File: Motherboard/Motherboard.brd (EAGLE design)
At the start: 87.5 x 150 mm, 11 parts

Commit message: refactor
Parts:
- moved J2 54.6 mm to (7.00, 127.0)
- moved J1 39.3 mm to (11.5, 95.5)
- moved U$1 39.3 mm to (19.7, 64.0)
- moved ARDUINO_NANO1 18.5 mm to (47.3, 74.8), turned to 90 degrees
- moved GPS2 6.32 mm to (53.4, 134.1)
- moved IMU 6.32 mm to (37.9, 110.2)
- moved R_SCL 6.32 mm to (16.4, 123.7)
- moved U$3 6.32 mm to (23.7, 123.9)
- moved U$4 6.32 mm to (23.7, 144.2)
- moved ALTIMETER2 6.32 mm to (29.0, 110.7)
- moved R_SDA 6.32 mm to (16.4, 126.9)
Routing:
- added copper zone on layer 1, net GND

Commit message: wip
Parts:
- added AIR_BRAKE: (no value), SparkFun-Connectors:1X03
- renumbered J2 to POWER_IN
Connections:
- removed net VIN: ARDUINO_NANO1.15
- new net N$3: AIR_BRAKE.2, ARDUINO_NANO1.15, POWER_IN.1
- new net N$4: AIR_BRAKE.3, ARDUINO_NANO1.24
- net GND: now also AIR_BRAKE.1, POWER_IN.2
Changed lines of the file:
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@@
 <?xml version="1.0" encoding="utf-8"?>
 <!DOCTYPE eagle SYSTEM "eagle.dtd">
-<eagle version="9.3.0">
+<eagle version="9.3.1">
 <drawing>
 <settings>
@@
 <attribute name="VALUE" x="10.23" y="93.087" size="0.6096" layer="27" font="vector" ratio="20"/>
 </element>
-<element name="J2" library="SparkFun-Connectors" package="SCREWTERMINAL-3.5MM-2" value="" x="7" y="127" smashed="yes" rot="R270">
+<element name="POWER_IN" library="SparkFun-Connectors" package="SCREWTERMINAL-3.5MM-2" value="" x="7" y="127" smashed="yes" rot="R270">
 <attribute name="NAME" x="9.54" y="128.27" size="0.6096" layer="25" font="vector" ratio="20" rot="R270"/>
 <attribute name="PROD_ID" value="CONN-08399" x="7" y="127" size="1.778" layer="27" rot="R270" display="off"/>
 <attribute name="VALUE" x="8.27" y="128.27" size="0.6096" layer="27" font="vector" ratio="20" rot="R270"/>
+</element>
+<element name="AIR_BRAKE" library="SparkFun-Connectors" package="1X03" value="" x="39.5" y="45" smashed="yes">
+<attribute name="NAME" x="38.23" y="46.397" size="0.6096" layer="25" font="vector" ratio="20"/>
+<attribute name="PROD_ID" value="XXX-00000" x="39.5" y="45" size="1.778" layer="27" display="off"/>
+<attribute name="VALUE" x="38.23" y="42.968" size="0.6096" layer="27" font="vector" ratio="20"/>
 </element>
 </elements>
@@
 <vertex x="0" y="0"/>
 </polygon>
+<contactref element="POWER_IN" pad="2"/>
+<contactref element="AIR_BRAKE" pad="1"/>
+<wire x1="40.41" y1="112.52" x2="53.378" y2="129.01" width="0" layer="19" extent="1-1"/>
 <wire x1="29.013" y1="110.69" x2="40.41" y2="112.52" width="0" layer="19" extent="1-1"/>
+<wire x1="7" y1="123.5" x2="29.013" y2="110.69" width="0" layer="19" extent="1-1"/>
+<wire x1="54.96" y1="87.51" x2="40.41" y2="112.52" width="0" layer="19" extent="1-1"/>
+<wire x1="39.72" y1="82.43" x2="54.96" y2="87.51" width="0" layer="19" extent="1-1"/>
+<wire x1="39.5" y1="45" x2="39.72" y2="82.43" width="0" layer="19" extent="1-1"/>
 </signal>
 <signal name="5V">
 <contactref element="ARDUINO_NANO1" pad="12"/>
-</signal>
-<signal name="VIN">
-<contactref element="ARDUINO_NANO1" pad="15"/>
 </signal>
 <signal name="3V3">
@@
 <wire x1="54.96" y1="74.81" x2="40.39" y2="117.43" width="0" layer="19" extent="1-1"/>
 </signal>
+<signal name="N$3">
+<contactref element="AIR_BRAKE" pad="2"/>
+<contactref element="POWER_IN" pad="1"/>
+<contactref element="ARDUINO_NANO1" pad="15"/>
+<wire x1="7" y1="127" x2="54.96" y2="90.05" width="0" layer="19" extent="1-1"/>
+<wire x1="42.04" y1="45" x2="54.96" y2="90.05" width="0" layer="19" extent="1-1"/>
+</signal>
+<signal name="N$4">
+<contactref element="AIR_BRAKE" pad="3"/>
+<contactref element="ARDUINO_NANO1" pad="24"/>
+<wire x1="44.58" y1="45" x2="39.72" y2="69.73" width="0" layer="19" extent="1-1"/>
+</signal>
 </signals>

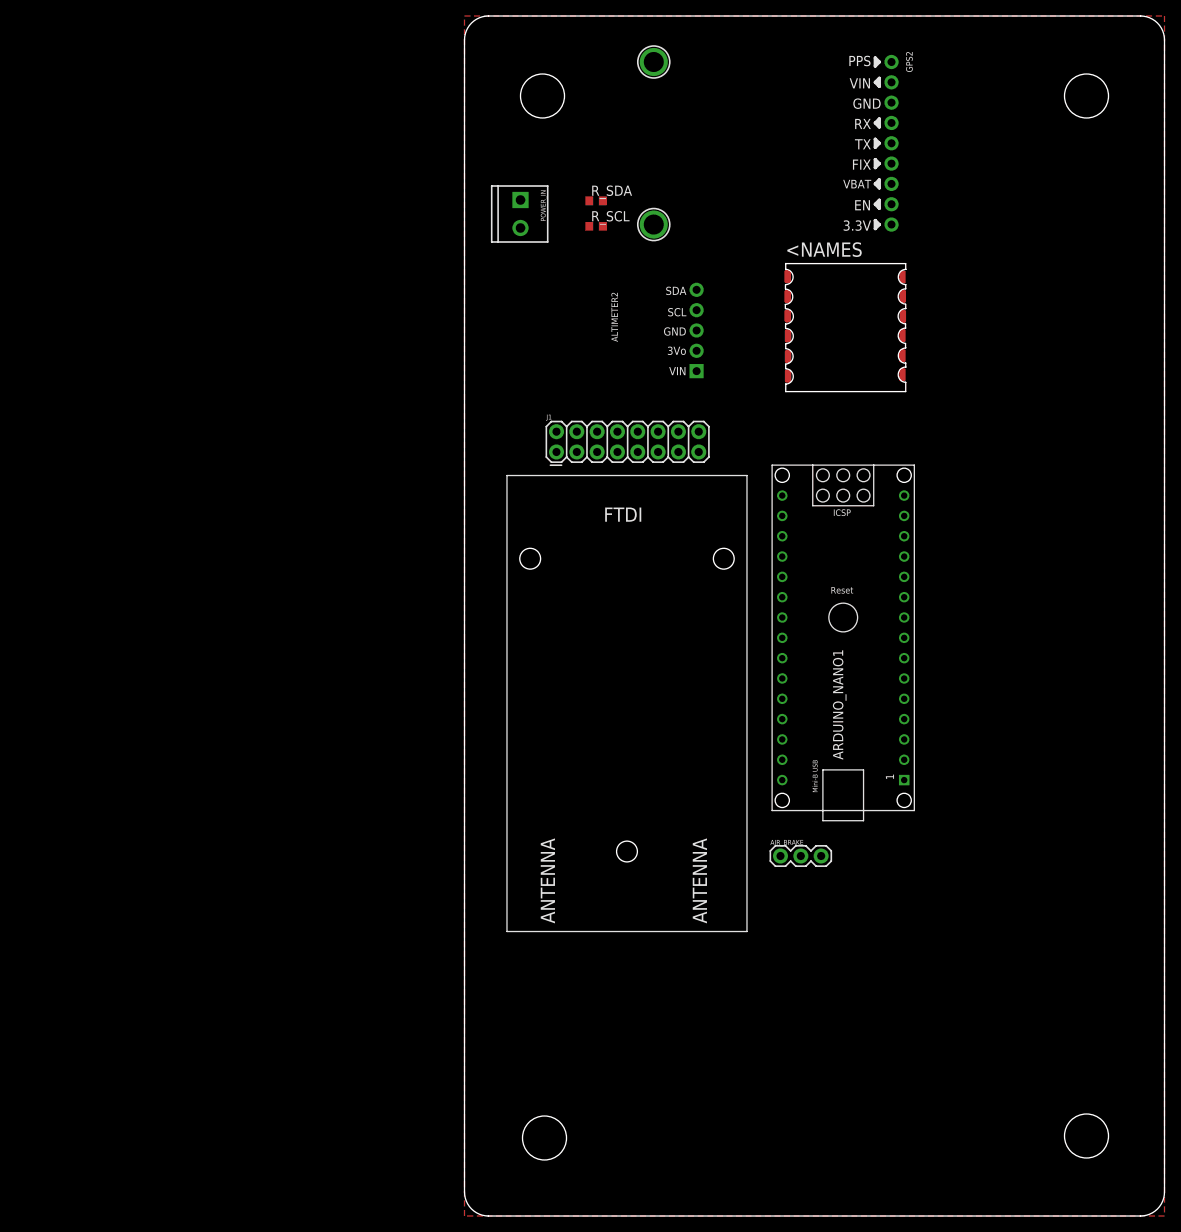
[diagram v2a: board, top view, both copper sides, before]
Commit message: add SD card, wire radio
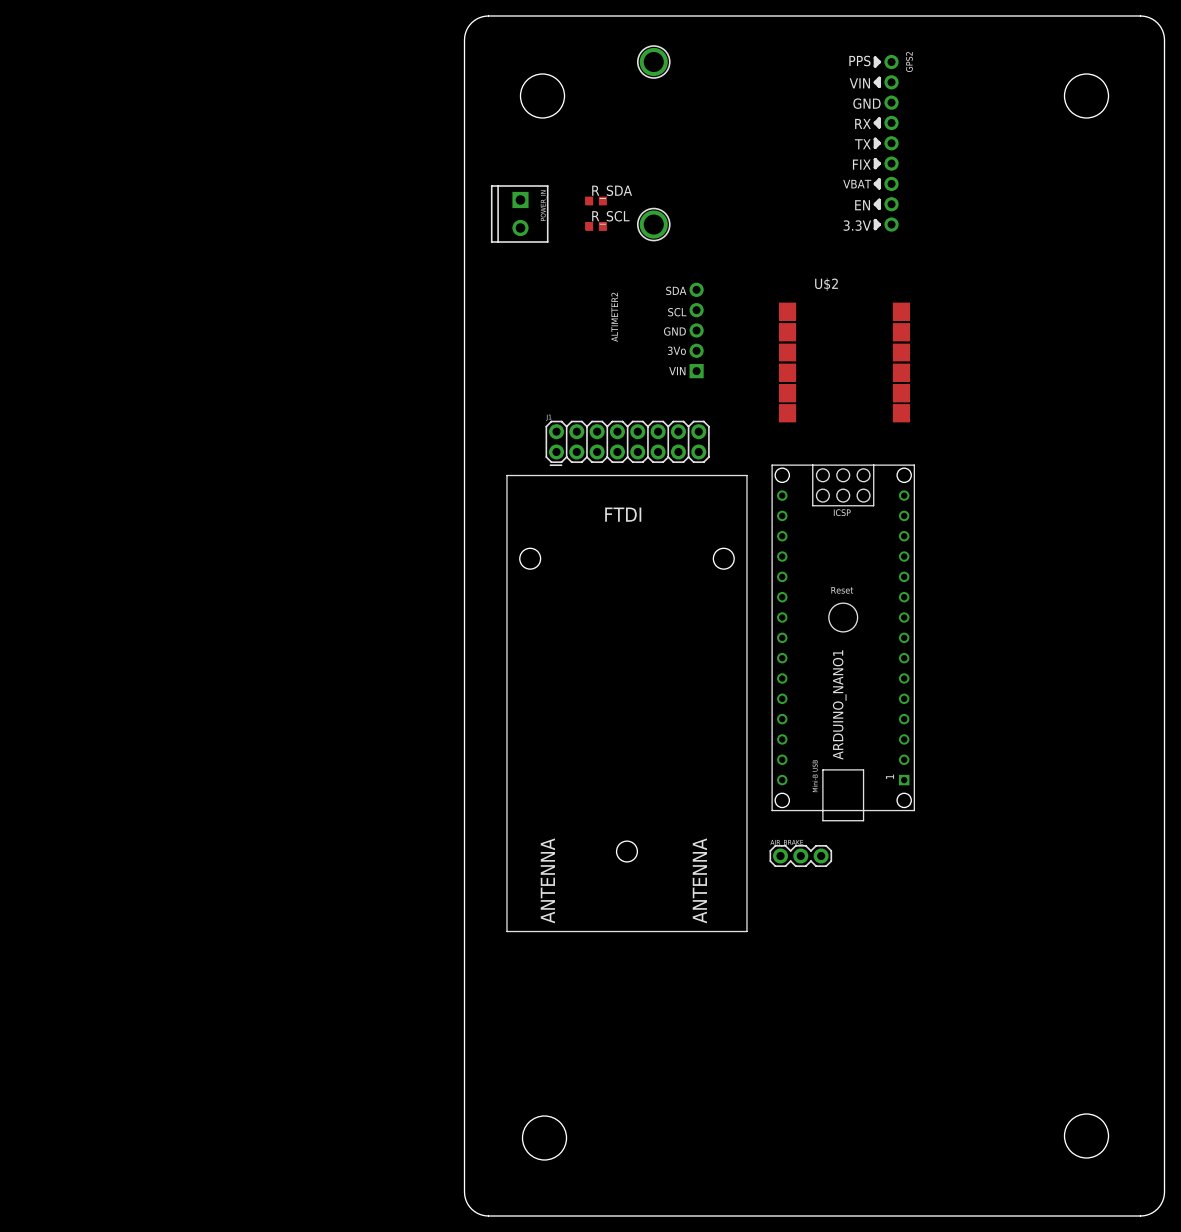
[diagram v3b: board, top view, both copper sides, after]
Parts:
- removed IMU: YOSTLABSIMU, YOST LABS IMU:YOSTLABSIMU
- added U$2: YOST, ArduinoNanoV30:YOST
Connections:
- removed net N$3: AIR_BRAKE.2, ARDUINO_NANO1.15, POWER_IN.1
- new net +5V: AIR_BRAKE.2, ARDUINO_NANO1.15, J1.6, POWER_IN.1
- new net RADIO_SHORT: J1.3, J1.5
- new net RX0: ARDUINO_NANO1.17, J1.10
- new net TX1: ARDUINO_NANO1.16, J1.8
- net 3V3: now also U$2.P$6; no longer IMU.VIN
- net GND: now also J1.2, U$2.P$3; no longer IMU.GND
- net SCL: now also U$2.P$1; no longer IMU.SCL
- net SDA: now also U$2.P$2; no longer IMU.SDA
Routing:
- removed copper zone on layer 1, net GND
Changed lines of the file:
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@@
 </class>
 </classes>
-<designrules name="default">
+<designrules name="default *">
 <description language="de">&lt;b&gt;EAGLE Design Rules&lt;/b&gt;
 &lt;p&gt;
@@
 <param name="mdDrill" value="6mil"/>
 <param name="mdSmdStop" value="0mil"/>
-<param name="msWidth" value="6mil"/>
+<param name="msWidth" value="30mil"/>
 <param name="msDrill" value="0.35mm"/>
 <param name="msMicroVia" value="9.99mm"/>
@@
 <attribute name="VALUE" x="49.88" y="57.03" size="1.27" layer="21" font="vector" rot="R90"/>
 </element>
-<element name="IMU" library="YOST LABS IMU" package="YOSTLABSIMU" value="YOSTLABSIMU" x="37.94" y="110.21" smashed="yes"/>
 <element name="R_SCL" library="rcl" library_urn="urn:adsk.eagle:library:334" package="R0603" package3d_urn="urn:adsk.eagle:package:23555/3" value="" x="16.44" y="123.7" smashed="yes">
 <attribute name="NAME" x="15.805" y="124.335" size="1.27" layer="25"/>
@@
 <attribute name="PROD_ID" value="XXX-00000" x="39.5" y="45" size="1.778" layer="27" display="off"/>
 <attribute name="VALUE" x="38.23" y="42.968" size="0.6096" layer="27" font="vector" ratio="20"/>
+</element>
+<element name="U$2" library="ArduinoNanoV30" package="YOST" value="YOST" x="47.5" y="107" smashed="yes">
+<attribute name="NAME" x="43.69" y="115.89" size="1.27" layer="25"/>
+<attribute name="VALUE" x="43.69" y="96.84" size="1.27" layer="27"/>
 </element>
 </elements>
@@
 <contactref element="ARDUINO_NANO1" pad="19"/>
 <contactref element="ARDUINO_NANO1" pad="14"/>
-<contactref element="IMU" pad="GND"/>
 <contactref element="GPS2" pad="7"/>
 <contactref element="ALTIMETER2" pad="3"/>
-<polygon width="0.1524" layer="1" thermals="no" rank="6">
-<vertex x="0" y="150"/>
-<vertex x="87.5" y="150"/>
-<vertex x="87.5" y="0"/>
-<vertex x="0" y="0"/>
-</polygon>
 <contactref element="POWER_IN" pad="2"/>
 <contactref element="AIR_BRAKE" pad="1"/>
-<wire x1="40.41" y1="112.52" x2="53.378" y2="129.01" width="0" layer="19" extent="1-1"/>
-<wire x1="29.013" y1="110.69" x2="40.41" y2="112.52" width="0" layer="19" extent="1-1"/>
+<contactref element="U$2" pad="P$3"/>
+<contactref element="J1" pad="2"/>
+<wire x1="40.3875" y1="107.937" x2="53.378" y2="129.01" width="0" layer="19" extent="1-1"/>
+<wire x1="29.013" y1="110.69" x2="40.3875" y2="107.937" width="0" layer="19" extent="1-1"/>
+<wire x1="11.5" y1="98.04" x2="29.013" y2="110.69" width="0" layer="19" extent="1-1"/>
+<wire x1="54.96" y1="87.51" x2="40.3875" y2="107.937" width="0" layer="19" extent="1-1"/>
+<wire x1="39.72" y1="82.43" x2="54.96" y2="87.51" width="0" layer="19" extent="1-1"/>
 <wire x1="7" y1="123.5" x2="29.013" y2="110.69" width="0" layer="19" extent="1-1"/>
-<wire x1="54.96" y1="87.51" x2="40.41" y2="112.52" width="0" layer="19" extent="1-1"/>
-<wire x1="39.72" y1="82.43" x2="54.96" y2="87.51" width="0" layer="19" extent="1-1"/>
 <wire x1="39.5" y1="45" x2="39.72" y2="82.43" width="0" layer="19" extent="1-1"/>
 </signal>
@@
 <signal name="3V3">
 <contactref element="ARDUINO_NANO1" pad="2"/>
-<contactref element="IMU" pad="VIN"/>
 <contactref element="R_SCL" pad="1"/>
 <contactref element="R_SDA" pad="1"/>
 <contactref element="GPS2" pad="1"/>
 <contactref element="ALTIMETER2" pad="1"/>
-<wire x1="40.45" y1="104.99" x2="53.378" y2="144.25" width="0" layer="19" extent="1-1"/>
-<wire x1="29.013" y1="105.61" x2="40.45" y2="104.99" width="0" layer="19" extent="1-1"/>
-<wire x1="15.59" y1="123.7" x2="29.013" y2="105.61" width="0" layer="19" extent="1-1"/>
-<wire x1="15.59" y1="126.89" x2="15.59" y2="123.7" width="0" layer="19" extent="1-1"/>
-<wire x1="54.96" y1="57.03" x2="40.45" y2="104.99" width="0" layer="19" extent="1-1"/>
+<contactref element="U$2" pad="P$6"/>
+<wire x1="15.59" y1="126.89" x2="53.378" y2="144.25" width="0" layer="19" extent="1-1"/>
+<wire x1="15.59" y1="123.7" x2="15.59" y2="126.89" width="0" layer="19" extent="1-1"/>
+<wire x1="29.013" y1="105.61" x2="15.59" y2="123.7" width="0" layer="19" extent="1-1"/>
+<wire x1="40.3875" y1="100.317" x2="29.013" y2="105.61" width="0" layer="19" extent="1-1"/>
+<wire x1="54.96" y1="57.03" x2="40.3875" y2="100.317" width="0" layer="19" extent="1-1"/>
 </signal>
 <signal name="TX">
@@
 <signal name="SDA">
 <contactref element="ARDUINO_NANO1" pad="8"/>
-<contactref element="IMU" pad="SDA"/>
 <contactref element="R_SDA" pad="2"/>
 <contactref element="ALTIMETER2" pad="5"/>
-<wire x1="29.013" y1="115.77" x2="40.4" y2="114.94" width="0" layer="19" extent="1-1"/>
+<contactref element="U$2" pad="P$2"/>
+<wire x1="29.013" y1="115.77" x2="40.3875" y2="110.477" width="0" layer="19" extent="1-1"/>
 <wire x1="17.29" y1="126.89" x2="29.013" y2="115.77" width="0" layer="19" extent="1-1"/>
-<wire x1="54.96" y1="72.27" x2="40.4" y2="114.94" width="0" layer="19" extent="1-1"/>
+<wire x1="54.96" y1="72.27" x2="40.3875" y2="110.477" width="0" layer="19" extent="1-1"/>
 </signal>
 <signal name="SCL">
 <contactref element="ARDUINO_NANO1" pad="9"/>
-<contactref element="IMU" pad="SCL"/>
 <contactref element="R_SCL" pad="2"/>
 <contactref element="ALTIMETER2" pad="4"/>
-<wire x1="29.013" y1="113.23" x2="40.39" y2="117.43" width="0" layer="19" extent="1-1"/>
+<contactref element="U$2" pad="P$1"/>
+<wire x1="29.013" y1="113.23" x2="40.3875" y2="113.017" width="0" layer="19" extent="1-1"/>
 <wire x1="17.29" y1="123.7" x2="29.013" y2="113.23" width="0" layer="19" extent="1-1"/>
-<wire x1="54.96" y1="74.81" x2="40.39" y2="117.43" width="0" layer="19" extent="1-1"/>
-</signal>
-<signal name="N$3">
+<wire x1="54.96" y1="74.81" x2="40.3875" y2="113.017" width="0" layer="19" extent="1-1"/>
+</signal>
+<signal name="+5V">
 <contactref element="AIR_BRAKE" pad="2"/>
 <contactref element="POWER_IN" pad="1"/>
 <contactref element="ARDUINO_NANO1" pad="15"/>
-<wire x1="7" y1="127" x2="54.96" y2="90.05" width="0" layer="19" extent="1-1"/>
+<contactref element="J1" pad="6"/>
+<wire x1="16.58" y1="98.04" x2="54.96" y2="90.05" width="0" layer="19" extent="1-1"/>
+<wire x1="7" y1="127" x2="16.58" y2="98.04" width="0" layer="19" extent="1-1"/>
 <wire x1="42.04" y1="45" x2="54.96" y2="90.05" width="0" layer="19" extent="1-1"/>
 </signal>
@@
 <wire x1="44.58" y1="45" x2="39.72" y2="69.73" width="0" layer="19" extent="1-1"/>
 </signal>
+<signal name="RADIO_SHORT">
+<contactref element="J1" pad="3"/>
+<contactref element="J1" pad="5"/>
+<wire x1="14.04" y1="95.5" x2="16.58" y2="95.5" width="0" layer="19" extent="1-1"/>
+</signal>
+<signal name="TX1">
+<contactref element="J1" pad="8"/>
+<contactref element="ARDUINO_NANO1" pad="16"/>
+<wire x1="19.12" y1="98.04" x2="39.72" y2="90.05" width="0" layer="19" extent="1-1"/>
+</signal>
+<signal name="RX0">
+<contactref element="J1" pad="10"/>
+<contactref element="ARDUINO_NANO1" pad="17"/>
+<wire x1="21.66" y1="98.04" x2="39.72" y2="87.51" width="0" layer="19" extent="1-1"/>
+</signal>
 </signals>

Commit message: library updates
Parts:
- added U$5: DFR0229, uORocketry-parts:DFR0229
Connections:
- net 5V: now also U$5.+5V
- net GND: now also U$5.GND
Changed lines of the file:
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@@
 <attribute name="VALUE" x="43.69" y="96.84" size="1.27" layer="27"/>
+</element>
+<element name="U$5" library="uORocketry-parts" package="DFR0229" value="DFR0229" x="-46" y="120" smashed="yes" rot="R180">
+<attribute name="NAME" x="-42.063" y="105.3188" size="1.27" layer="25" rot="R180"/>
+<attribute name="VALUE" x="-42.5202" y="135.8496" size="1.27" layer="27" rot="R180"/>
 </element>
 </elements>
@@
 <contactref element="U$2" pad="P$3"/>
 <contactref element="J1" pad="2"/>
+<contactref element="U$5" pad="GND"/>
 <wire x1="40.3875" y1="107.937" x2="53.378" y2="129.01" width="0" layer="19" extent="1-1"/>
 <wire x1="29.013" y1="110.69" x2="40.3875" y2="107.937" width="0" layer="19" extent="1-1"/>
@@
 <wire x1="7" y1="123.5" x2="29.013" y2="110.69" width="0" layer="19" extent="1-1"/>
 <wire x1="39.5" y1="45" x2="39.72" y2="82.43" width="0" layer="19" extent="1-1"/>
-</signal>
-<signal name="5V">
-<contactref element="ARDUINO_NANO1" pad="12"/>
+<wire x1="-50.56" y1="131.25" x2="7" y2="123.5" width="0" layer="19" extent="1-1"/>
 </signal>
 <signal name="3V3">
@@
 <wire x1="21.66" y1="98.04" x2="39.72" y2="87.51" width="0" layer="19" extent="1-1"/>
 </signal>
+<signal name="5V">
+<contactref element="ARDUINO_NANO1" pad="12"/>
+<contactref element="U$5" pad="+5V"/>
+<wire x1="-53.1" y1="131.25" x2="54.96" y2="82.43" width="0" layer="19" extent="1-1"/>
+</signal>
 </signals>
